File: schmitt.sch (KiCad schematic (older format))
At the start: 4 parts, among them U11 LM311

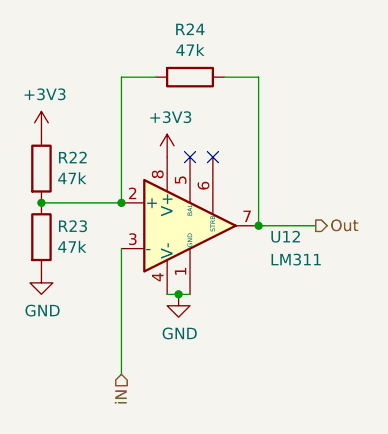
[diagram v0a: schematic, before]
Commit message: Add servos and can brush motor
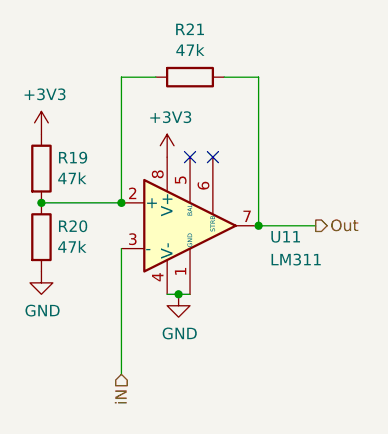
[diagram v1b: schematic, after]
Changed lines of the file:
@@
 AR Path="/5F2542FC/5F275DFF/5F137B8A" Ref="U11"  Part="1"
 AR Path="/5F2542FC/5F2E268E/5F137B8A" Ref="U12"  Part="1"
-F 0 "U12" H 5800 4100 50  0000 L CNN
+F 0 "U11" H 5800 4100 50  0000 L CNN
 F 1 "LM311" H 5800 4000 50  0000 L CNN
 F 2 "" H 5450 4150 50  0001 C CNN
@@
 AR Path="/5F2542FC/5F275DFF/5F138774" Ref="R21"  Part="1"
 AR Path="/5F2542FC/5F2E268E/5F138774" Ref="R24"  Part="1"
-F 0 "R24" V 5243 3500 50  0000 C CNN
+F 0 "R21" V 5243 3500 50  0000 C CNN
 F 1 "47k" V 5334 3500 50  0000 C CNN
 F 2 "" V 5380 3500 50  0001 C CNN
@@
 AR Path="/5F2542FC/5F275DFF/5F138BF8" Ref="R19"  Part="1"
 AR Path="/5F2542FC/5F2E268E/5F138BF8" Ref="R22"  Part="1"
-F 0 "R22" H 4870 3946 50  0000 L CNN
+F 0 "R19" H 4870 3946 50  0000 L CNN
 F 1 "47k" H 4870 3855 50  0000 L CNN
 F 2 "" V 4730 3900 50  0001 C CNN
@@
 AR Path="/5F2542FC/5F275DFF/5F138FD9" Ref="R20"  Part="1"
 AR Path="/5F2542FC/5F2E268E/5F138FD9" Ref="R23"  Part="1"
-F 0 "R23" H 4870 4246 50  0000 L CNN
+F 0 "R20" H 4870 4246 50  0000 L CNN
 F 1 "47k" H 4870 4155 50  0000 L CNN
 F 2 "" V 4730 4200 50  0001 C CNN

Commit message: Misc minor fixes
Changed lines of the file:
@@
 $Descr A4 11693 8268
 encoding utf-8
-Sheet 5 6
+Sheet 6 6
 Title ""
 Date ""
@@
 AR Path="/5F2542FC/5F275DFF/5F137B8A" Ref="U11"  Part="1"
 AR Path="/5F2542FC/5F2E268E/5F137B8A" Ref="U12"  Part="1"
-F 0 "U11" H 5800 4100 50  0000 L CNN
+F 0 "U12" H 5800 4100 50  0000 L CNN
 F 1 "LM311" H 5800 4000 50  0000 L CNN
 F 2 "" H 5450 4150 50  0001 C CNN
@@
 AR Path="/5F2542FC/5F275DFF/5F138774" Ref="R21"  Part="1"
 AR Path="/5F2542FC/5F2E268E/5F138774" Ref="R24"  Part="1"
-F 0 "R21" V 5243 3500 50  0000 C CNN
+F 0 "R24" V 5243 3500 50  0000 C CNN
 F 1 "47k" V 5334 3500 50  0000 C CNN
 F 2 "" V 5380 3500 50  0001 C CNN
@@
 AR Path="/5F2542FC/5F275DFF/5F138BF8" Ref="R19"  Part="1"
 AR Path="/5F2542FC/5F2E268E/5F138BF8" Ref="R22"  Part="1"
-F 0 "R19" H 4870 3946 50  0000 L CNN
+F 0 "R22" H 4870 3946 50  0000 L CNN
 F 1 "47k" H 4870 3855 50  0000 L CNN
 F 2 "" V 4730 3900 50  0001 C CNN
@@
 AR Path="/5F2542FC/5F275DFF/5F138FD9" Ref="R20"  Part="1"
 AR Path="/5F2542FC/5F2E268E/5F138FD9" Ref="R23"  Part="1"
-F 0 "R20" H 4870 4246 50  0000 L CNN
+F 0 "R23" H 4870 4246 50  0000 L CNN
 F 1 "47k" H 4870 4155 50  0000 L CNN
 F 2 "" V 4730 4200 50  0001 C CNN
